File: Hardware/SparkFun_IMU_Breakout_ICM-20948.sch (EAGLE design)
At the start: 36 parts, among them U1 9DoF IMU, U2 TXB0108DQSR

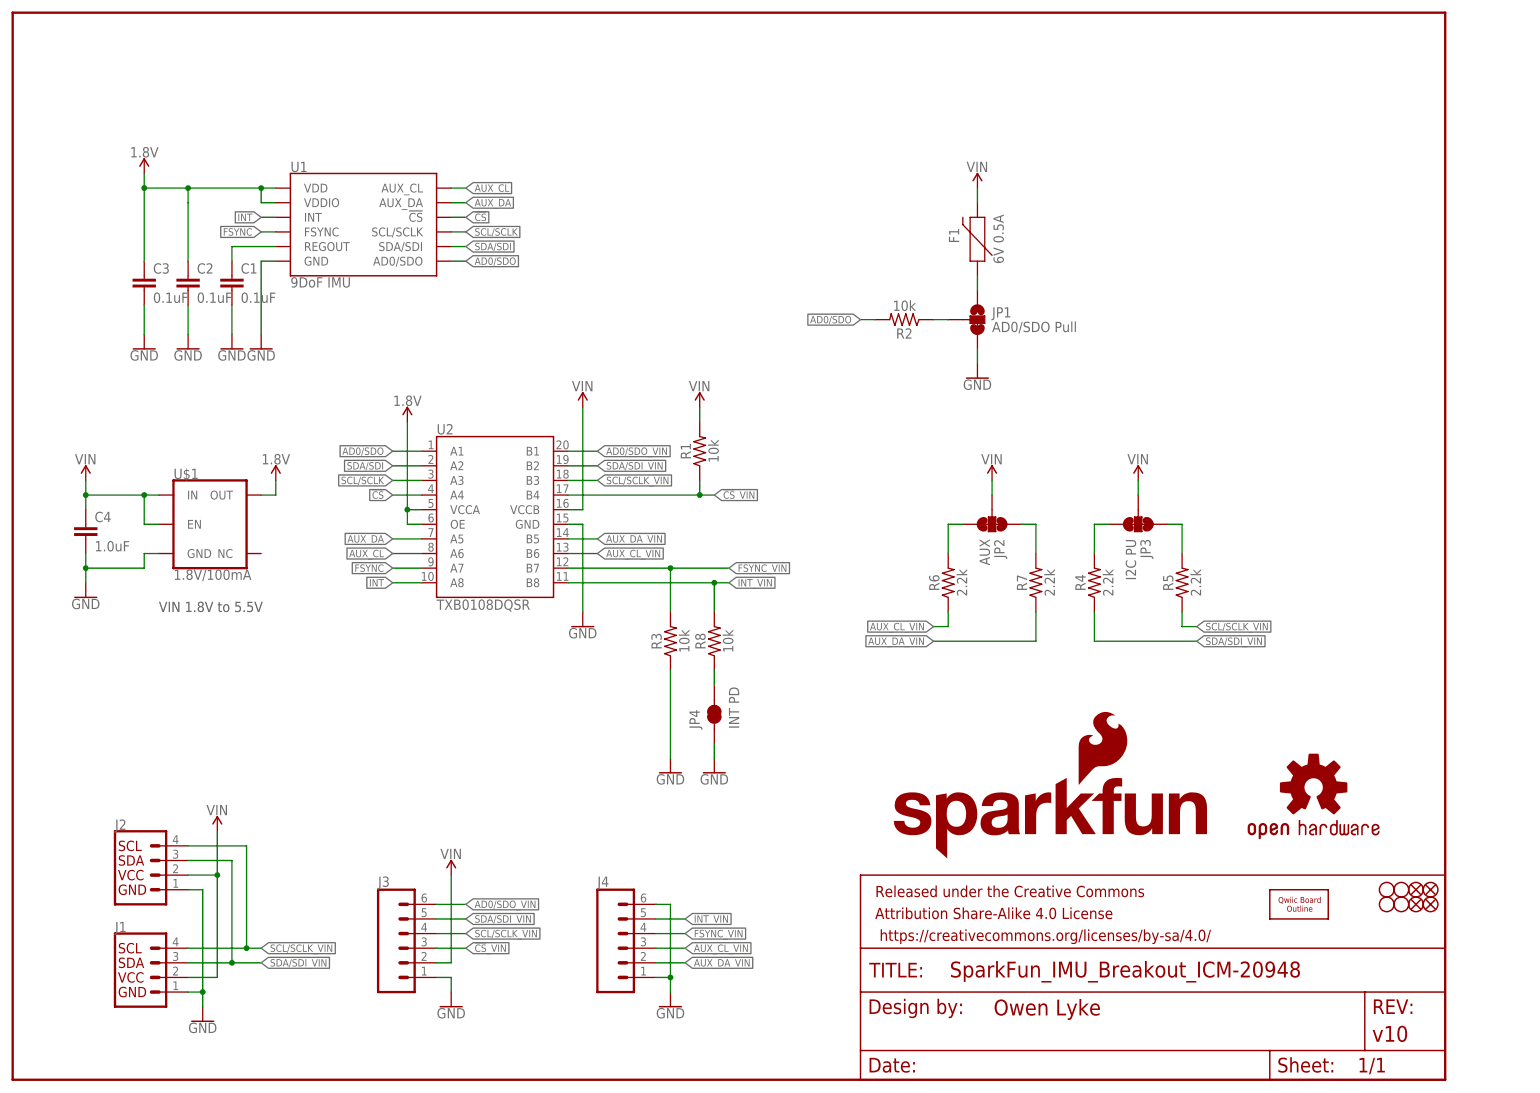
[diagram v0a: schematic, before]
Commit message: Prettified the schematic
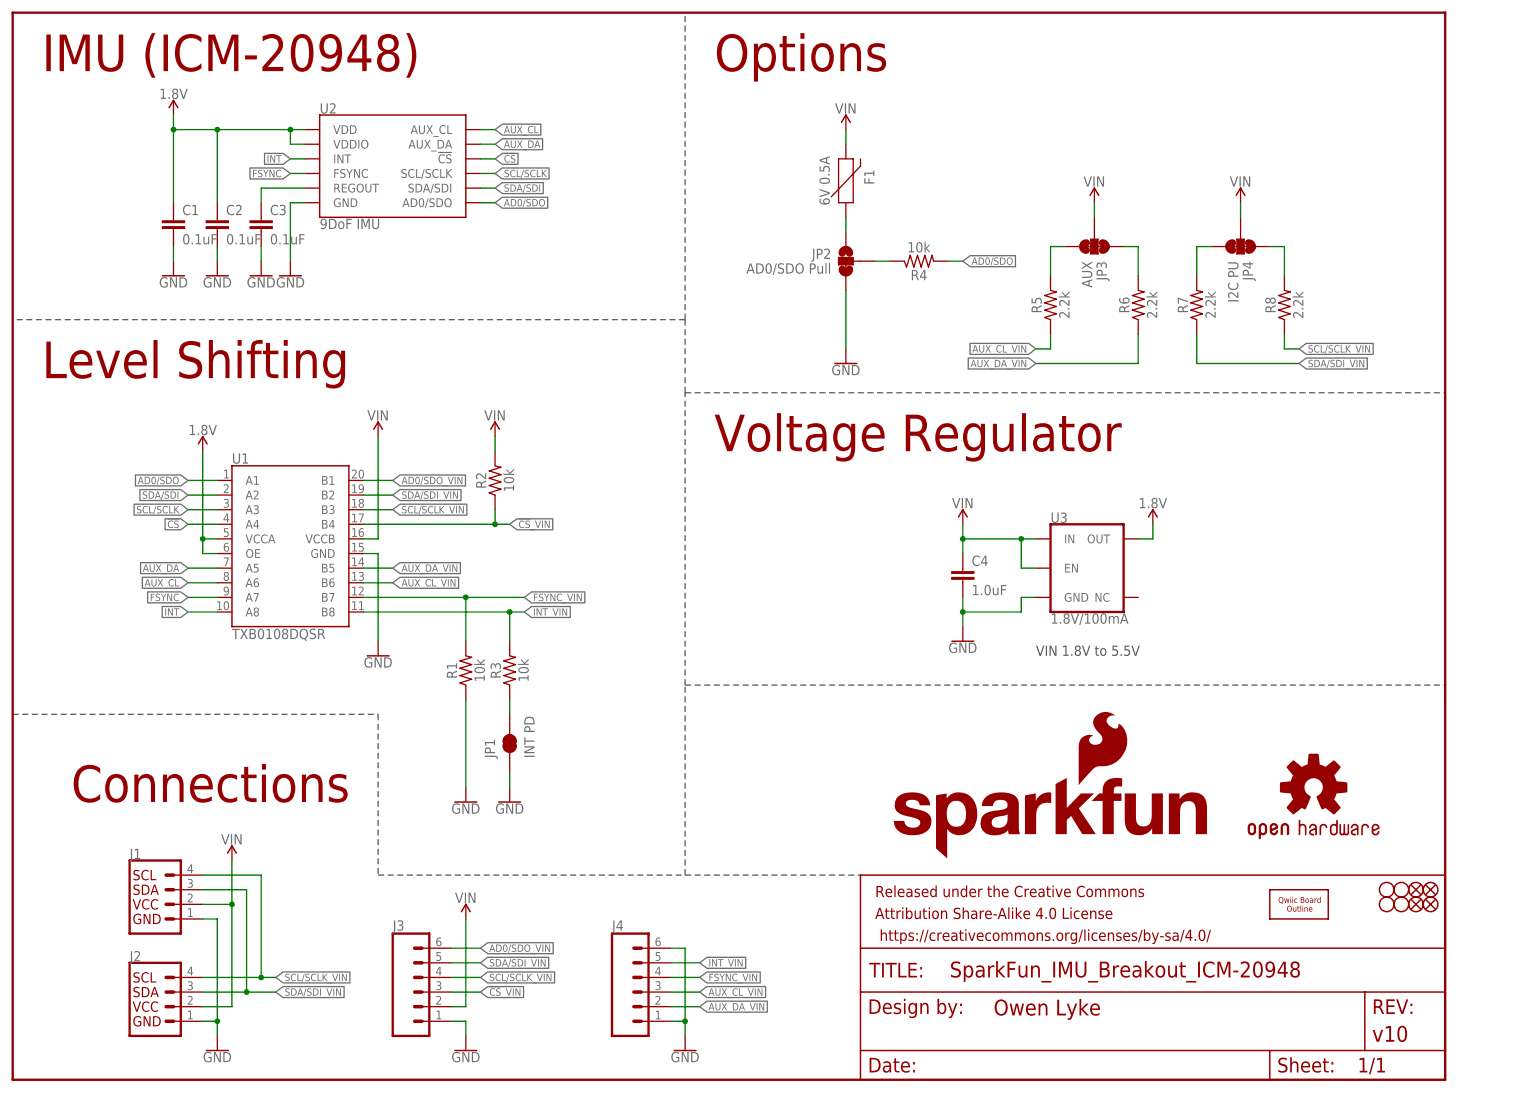
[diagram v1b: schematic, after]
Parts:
- removed U$1: 1.8V/100mA, SparkFun-IC-Power:V_REG_SP6214-1.8V
- added U3: 1.8V/100mA, SparkFun-IC-Power:V_REG_SP6214-1.8V
- JP1: value AD0/SDO Pull -> INT PD; device SparkFun-Jumpers:JUMPER-SMT_3_1-NC_TRACE_SILK -> SparkFun-Jumpers:JUMPER-SMT_2_NC_TRACE_SILK
- JP2: value AUX -> AD0/SDO Pull; device SparkFun-Jumpers:JUMPER-SMT_3_2-NC_TRACE_SILK -> SparkFun-Jumpers:JUMPER-SMT_3_1-NC_TRACE_SILK
- JP3: value I2C PU -> AUX
- JP4: value INT PD -> I2C PU; device SparkFun-Jumpers:JUMPER-SMT_2_NC_TRACE_SILK -> SparkFun-Jumpers:JUMPER-SMT_3_2-NC_TRACE_SILK
- R4: value 2.2k -> 10k; device SparkFun-Resistors:2.2KOHM-0603-1/10W-1% -> SparkFun-Resistors:10KOHM-0603-1/10W-1%
- R8: value 10k -> 2.2k; device SparkFun-Resistors:10KOHM-0603-1/10W-1% -> SparkFun-Resistors:2.2KOHM-0603-1/10W-1%
- U1: value 9DoF IMU -> TXB0108DQSR; device SparkFun-Sensors:ICM-20948 -> SparkFun-IC-Comms:TXB0108
- U2: value TXB0108DQSR -> 9DoF IMU; device SparkFun-IC-Comms:TXB0108 -> SparkFun-Sensors:ICM-20948
- renumbered U$2 to A1
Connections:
- net !CS: now also U1.A4, U2.!CS; no longer U1.!CS, U2.A4
- net !CS!_VIN: now also R2.1, U1.B4; no longer R1.1, U2.B4
- net 1.8V: now also C1.1, U1.OE, U1.VCCA, U2.VDD, U2.VDDIO, U3.OUT; no longer C3.1, U$1.OUT, U1.VDD, U1.VDDIO, U2.OE, U2.VCCA
- net AD0/SDO: now also R4.2, U1.A1, U2.AD0/SDO; no longer R2.2, U1.AD0/SDO, U2.A1
- net AD0/SDO_VIN: now also U1.B1; no longer U2.B1
- net AUX_CL: now also U1.A6, U2.AUX_CL; no longer U1.AUX_CL, U2.A6
- net AUX_CL_VIN: now also R5.1, U1.B6; no longer R6.1, U2.B6
- net AUX_DA: now also U1.A5, U2.AUX_DA; no longer U1.AUX_DA, U2.A5
- net AUX_DA_VIN: now also R6.1, U1.B5; no longer R7.1, U2.B5
- net FSYNC: now also U1.A7, U2.FSYNC; no longer U1.FSYNC, U2.A7
- net FSYNC_VIN: now also R1.2, U1.B7; no longer R3.2, U2.B7
- net GND: now also JP1.1, JP2.3, R1.1, U3.GND; no longer JP1.3, JP4.1, R3.1, U$1.GND
- net INT: now also U1.A8, U2.INT; no longer U1.INT, U2.A8
- net INT_VIN: now also R3.2, U1.B8; no longer R8.2, U2.B8
- net N$1: now also C3.1, U2.REGOUT; no longer C1.1, U1.REGOUT
- net N$2: now also JP2.1; no longer JP1.1
- net N$3: now also JP2.2, R4.1; no longer JP1.2, R2.1
- net N$4: now also JP4.3, R7.2; no longer JP3.3, R4.2
- net N$5: now also JP4.1, R8.2; no longer JP3.1, R5.2
- net N$6: now also JP3.3, R5.2; no longer JP2.3, R6.2
- net N$7: now also JP3.1, R6.2; no longer JP2.1, R7.2
- net N$8: now also JP1.2, R3.1; no longer JP4.2, R8.1
- net SCL/SCLK: now also U1.A3, U2.SCL/SCLK; no longer U1.SCL/SCLK, U2.A3
- net SCL/SCLK_VIN: now also R8.1, U1.B3; no longer R5.1, U2.B3
- net SDA/SDI: now also U1.A2, U2.SDA/SDI; no longer U1.SDA/SDI, U2.A2
- net SDA/SDI_VIN: now also R7.1, U1.B2; no longer R4.1, U2.B2
- net VIN: now also JP4.2, R2.2, U1.VCCB, U3.EN, U3.IN; no longer JP2.2, R1.2, U$1.EN, U$1.IN, U2.VCCB
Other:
- note added: "Connections"
- note added: "IMU (ICM-20948)"
- note added: "Level Shifting"
- note added: "Options"
- note added: "Voltage Regulator"
- moved on the sheet: C1, C2, C3, C4, F1, J1, J2, J3, J4, JP3, R1, R2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

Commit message: Push to work from laptop
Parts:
- removed F1: 6V 0.5A, SparkFun-Fuses:PPTC_6V500MA
- added D1: RED, SparkFun-LED:LED-RED0603
- added JP5: LED, SparkFun-Jumpers:JUMPER-SMT_2_NC_TRACE_SILK
- added R9: 470, SparkFun-Resistors:470OHM-0603-1/10W-1%
- JP2: value AD0/SDO Pull -> AD0; device SparkFun-Jumpers:JUMPER-SMT_3_1-NC_TRACE_SILK -> SparkFun-Jumpers:JUMPER-SMT_2_NO_SILK
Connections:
- removed net N$2: F1.1, JP2.1
- removed net N$3: JP2.2, R4.1
- new net N$10: JP5.2, R9.1
- new net N$9: D1.C, R9.2
- net 1.8V: now also D1.A
- net AD0/SDO: no longer R4.2
- net AD0/SDO_VIN: now also JP2.2, R4.1
- net GND: now also JP2.1, JP5.1; no longer JP2.3
- net VIN: now also R4.2; no longer F1.2
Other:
- note added: "AD0 -> I2C Address open -> 0b1101001 closed -> 0b110100 *Closing AD0 precludes SPI"
- note added: "Optionally disconnect the I2C pullup resistors on the primary and auxillary busses in case of too strong pullup from other sources"
- moved on the sheet: JP3, JP4, R4, R5, R6, R7, R8

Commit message: Trace routing changes during design review
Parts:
- removed A1: QWIIC_BOARD_OUTLINENH, SparkX:QWIIC_BOARD_OUTLINENH

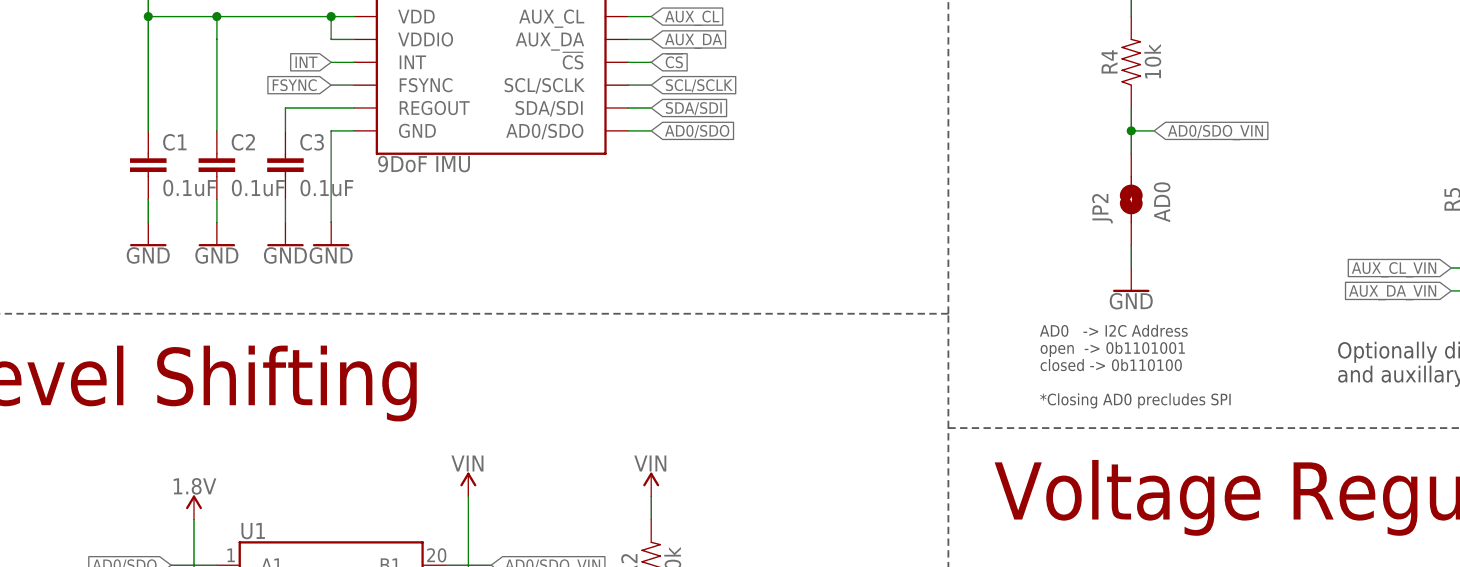
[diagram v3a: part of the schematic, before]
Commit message: Fixes notes from issue #1
In response to issue #1 I have:
- Replaced an existing 0.1 uF cap with 1.0 uF
- Changed address references to hex in .sch
- Questioned why we worry about vector font now that we use Buzzard
- Tried LED at 1.8V w and w/o CL resistor (1k). All is well
- Fixed all silk issues
- Research indicates that copper is not ferromagnetic (instead it is dimagnetic) so not a concern for the magnetometer
- Moved triple jumpers away from obstacles
- Slightly improved ground pour connectivity
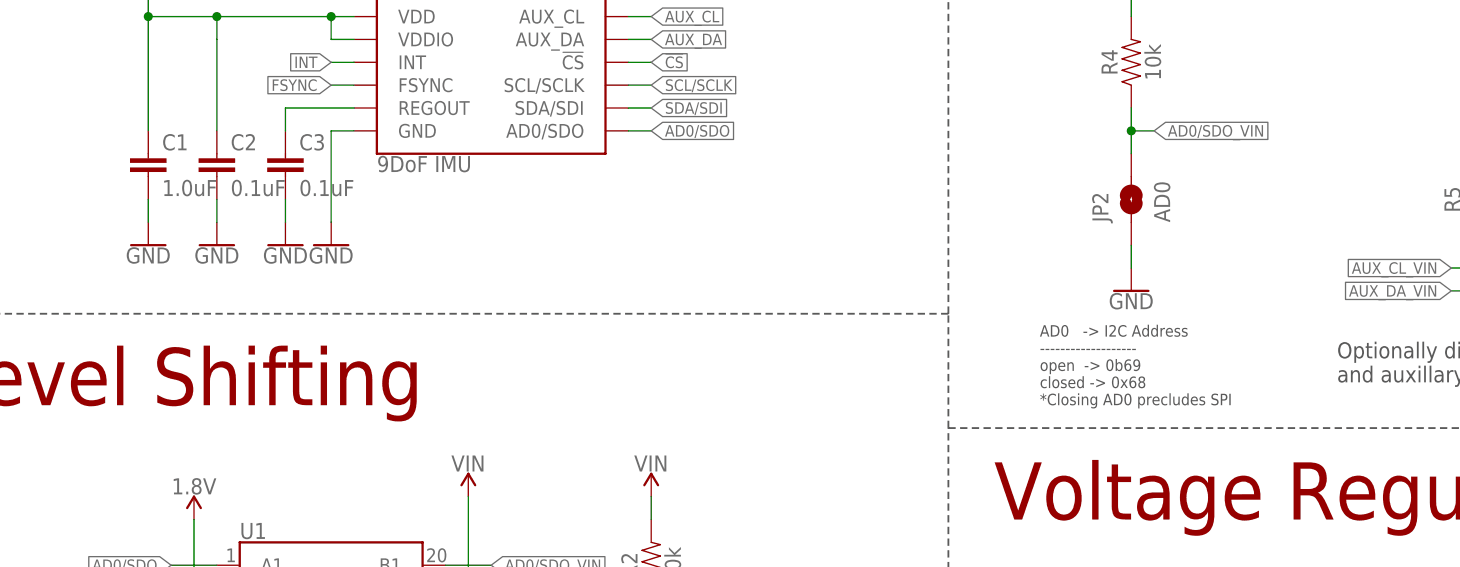
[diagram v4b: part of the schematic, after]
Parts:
- C1: value 0.1uF -> 1.0uF; device SparkFun-Capacitors:0.1UF-0603-25V-5% -> SparkFun-Capacitors:1.0UF-0603-16V-10%-X7R
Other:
- note added: "AD0 -> I2C Address ------------------- open -> 0b69 closed -> 0x68 *Closing AD0 precludes SPI"
- note removed: "AD0 -> I2C Address open -> 0b1101001 closed -> 0b110100 *Closing AD0 precludes SPI"
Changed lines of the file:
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@@
 <?xml version="1.0" encoding="utf-8"?>
 <!DOCTYPE eagle SYSTEM "eagle.dtd">
-<eagle version="9.2.0">
+<eagle version="9.1.3">
 <drawing>
 <settings>
-<setting alwaysvectorfont="no"/>
+<setting alwaysvectorfont="yes"/>
 <setting verticaltext="up"/>
 </settings>
@@
 <part name="C3" library="SparkFun-Capacitors" deviceset="0.1UF" device="-0603-25V-5%" value="0.1uF"/>
 <part name="C2" library="SparkFun-Capacitors" deviceset="0.1UF" device="-0603-25V-5%" value="0.1uF"/>
-<part name="C1" library="SparkFun-Capacitors" deviceset="0.1UF" device="-0603-25V-5%" value="0.1uF"/>
+<part name="C1" library="SparkFun-Capacitors" deviceset="1.0UF" device="-0603-16V-10%-X7R" value="1.0uF"/>
 <part name="GND5" library="SparkFun-PowerSymbols" deviceset="GND" device=""/>
 <part name="GND4" library="SparkFun-PowerSymbols" deviceset="GND" device=""/>
@@
 <wire x1="116.84" y1="132.08" x2="116.84" y2="185.42" width="0.2032" layer="97" style="longdash"/>
 <text x="127" y="121.92" size="1.27" layer="97">AD0   -&gt; I2C Address
-open  -&gt; 0b1101001
-closed -&gt; 0b110100
+-------------------
+open  -&gt; 0b69
+closed -&gt; 0x68
 *Closing AD0 precludes SPI</text>
 <text x="160.02" y="124.46" size="1.778" layer="97">Optionally disconnect the I2C pullup resistors on the primary

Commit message: Add PWR LED and axes labels
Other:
- note added: "AD0 -> I2C Address ------------------- open -> 0x69 closed -> 0x68 *Closing AD0 precludes SPI"
- note added: "Cut to disable PWR LED"
- note added: "Cut to release INT pulldown"
- note removed: "AD0 -> I2C Address ------------------- open -> 0b69 closed -> 0x68 *Closing AD0 precludes SPI"
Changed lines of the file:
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@@
 <text x="127" y="121.92" size="1.27" layer="97">AD0   -&gt; I2C Address
 -------------------
-open  -&gt; 0b69
+open  -&gt; 0x69
 closed -&gt; 0x68
 *Closing AD0 precludes SPI</text>
 <text x="160.02" y="124.46" size="1.778" layer="97">Optionally disconnect the I2C pullup resistors on the primary
 and auxillary busses in case of too strong pullup from other sources </text>
+<text x="226.06" y="78.74" size="1.27" layer="97">Cut to disable
+PWR LED</text>
+<text x="93.98" y="55.88" size="1.27" layer="97">Cut to release
+INT pulldown</text>
 </plain>
 <instances>
